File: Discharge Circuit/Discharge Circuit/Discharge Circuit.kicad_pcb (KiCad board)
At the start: 2 copper layers, 45.9 x 60.4 mm, 4 parts, among them J1 MPT-02-01-XX-X-RA-SD, J2 IPBT-102-H1-T-S-RA-K, J3 PET-02-XX-X-VT-LC, K1 DBT71210

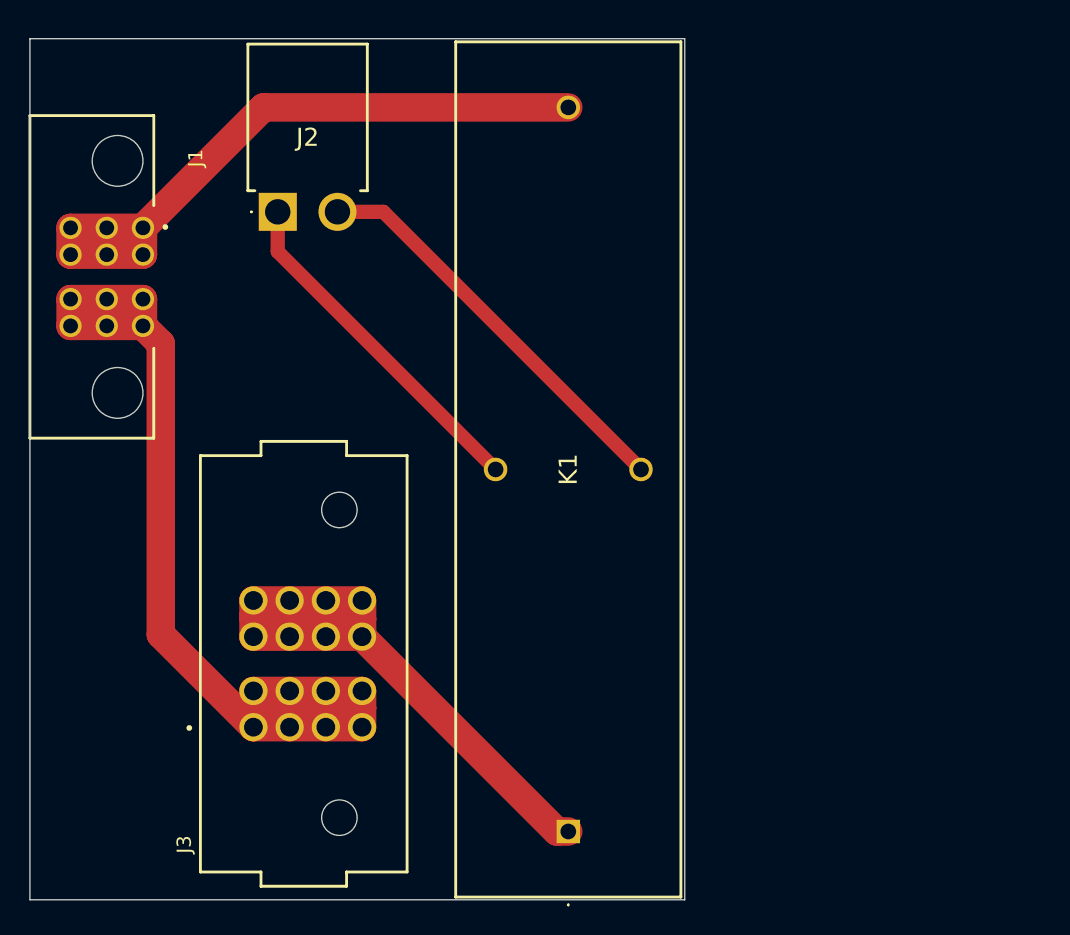
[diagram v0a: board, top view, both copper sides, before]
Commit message: New relay, added holes
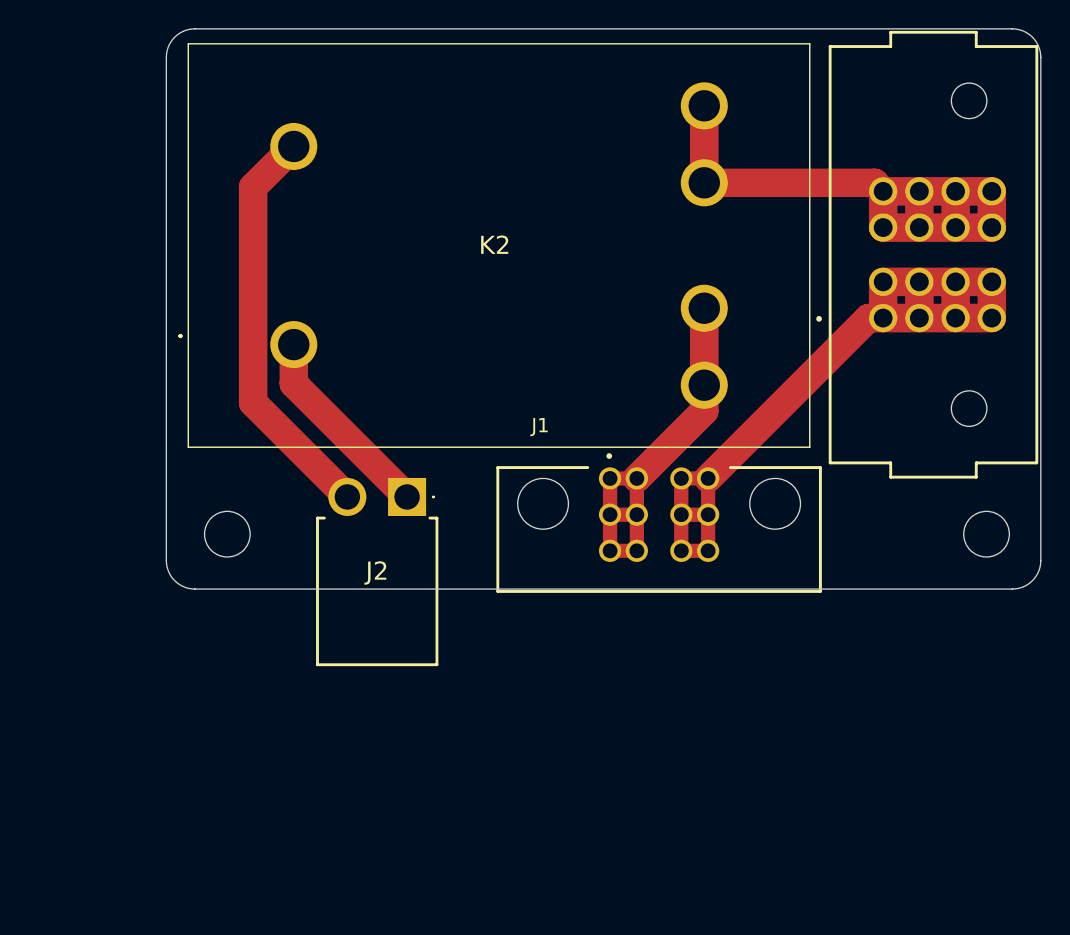
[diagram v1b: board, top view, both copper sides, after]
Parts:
- removed K1: DBT71210, DBT:DBT71210
- added H1: MountingHole, MountingHole:MountingHole_3.2mm_M3, F.Cu at (157.4, 123.8)
- added H2: MountingHole, MountingHole:MountingHole_3.2mm_M3, F.Cu at (104.1, 123.8)
- added K2: FTR-E1AA012Y-GR, FTR-E1AA012Y-GR:FTRE1AA012YGR, F.Cu at (108.8, 110.5)
- J3: value PET-02-XX-X-VT-LC -> PET-02-01-T-VT-LC
- moved J3 53.0 mm to (154.2, 104.3)
- moved J1 49.4 mm to (134.4, 127.8), turned to 0 degrees
- moved J2 22.0 mm to (116.7, 121.2), turned to 180 degrees
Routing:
- net Net-(J1-Pad2): track 78.3 -> 58.1 mm
- net Net-(K2-NO_1_1): track 47.3 -> 29.7 mm
- net Net-(K2-+): track 24.4 -> 14.0 mm
- net Net-(K2-NO_2_1): track 53.2 -> 43.6 mm
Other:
- board size 45.9 x 60.4 mm -> 61.3 x 39.3 mm

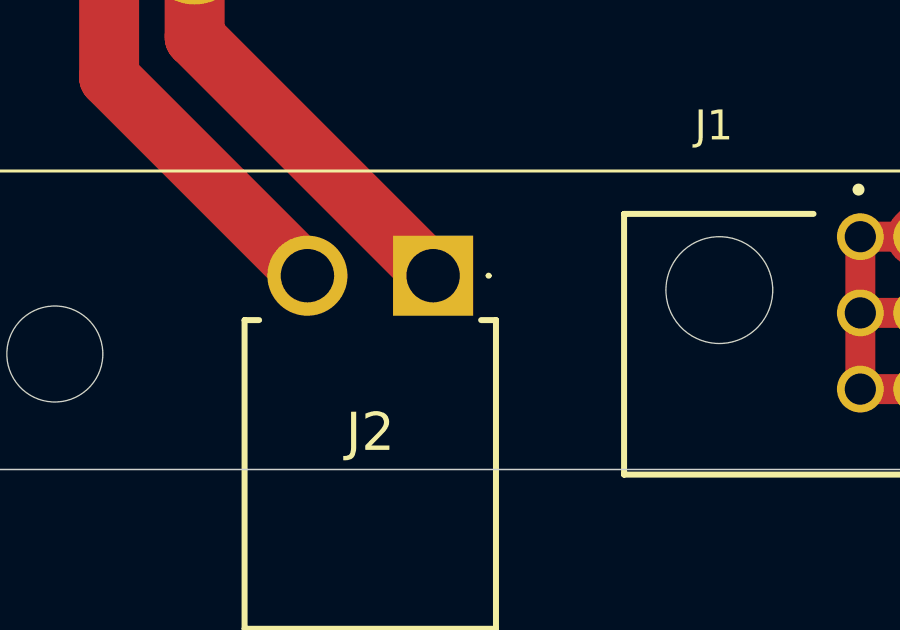
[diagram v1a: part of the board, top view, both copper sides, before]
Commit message: Added flyback diode
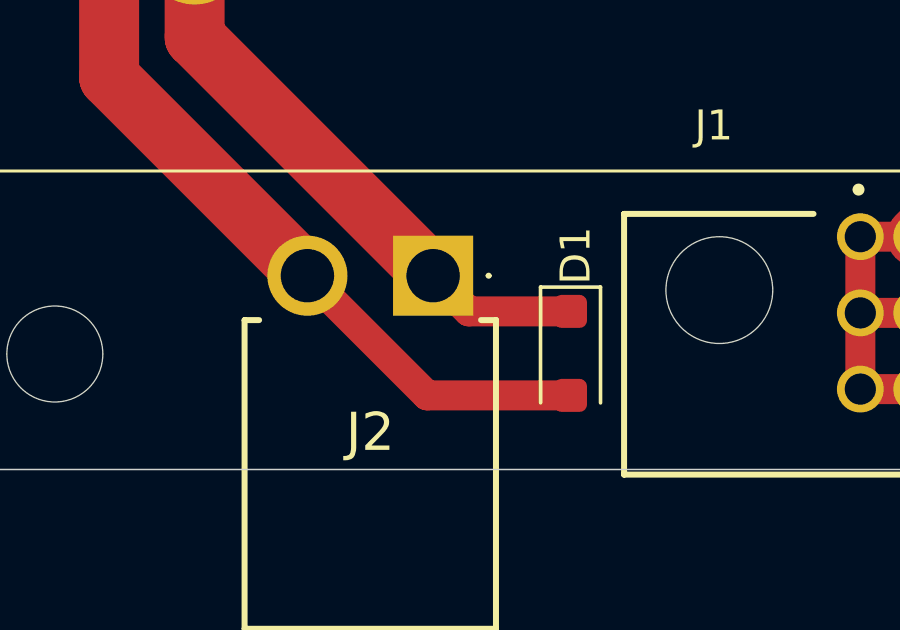
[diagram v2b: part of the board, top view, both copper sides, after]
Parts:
- added D1: 1N4007FL, Diode_SMD:D_SOD-123F, F.Cu at (121.3, 123.8)
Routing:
- net GND: track 28.5 -> 38.9 mm
- net Net-(D1-K): track 14.0 -> 19.1 mm
